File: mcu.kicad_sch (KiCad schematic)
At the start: 38 parts, among them SW1 SW_Push, SW2 SW_Push, SW3 SW_Push, SW4 SW_Push, U1 STM32H723VGTx, U13 BMI323, U14 AS5047P-ATST, U15 TCAN1044VDRQ1, X1 8MHz

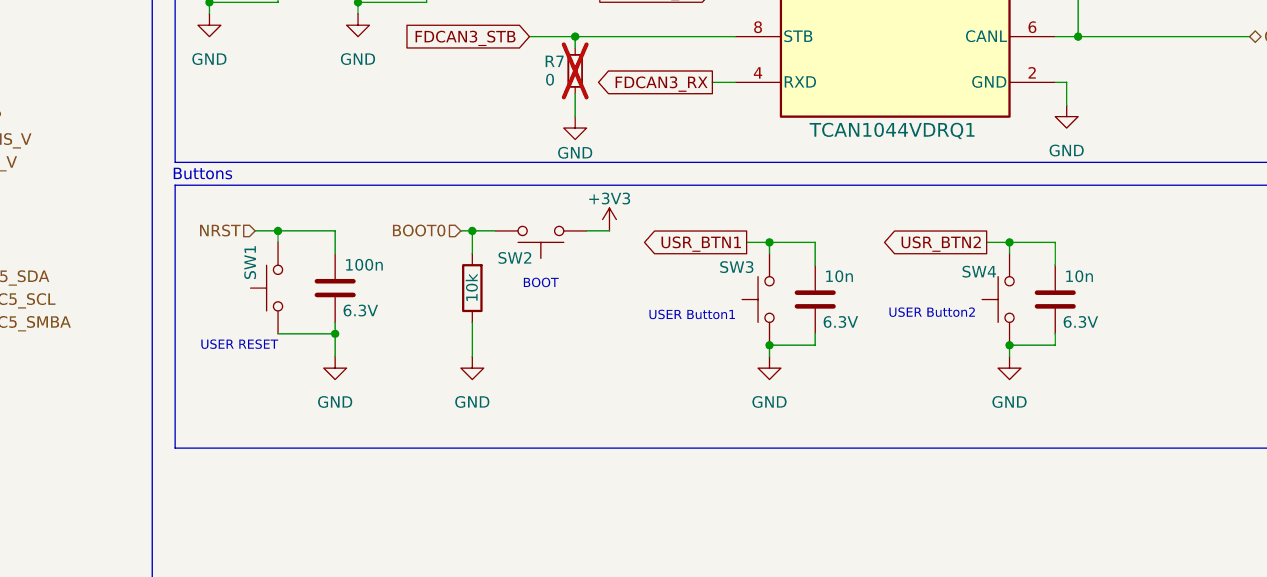
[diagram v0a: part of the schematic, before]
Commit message: Analog current filters were removed, some footprints were fixed and initial rough layout has been made.
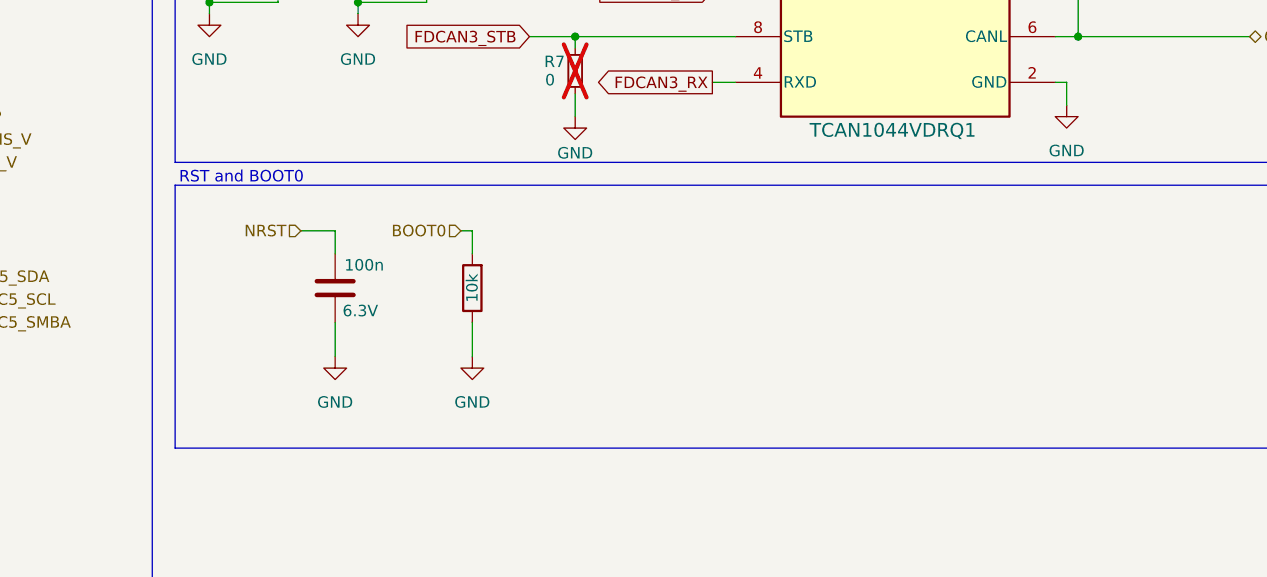
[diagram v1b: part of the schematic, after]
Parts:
- removed C81, C82: 10n, Capacitor_SMD:C_0201_0603Metric, symbol Device:C
- removed SW1, SW2, SW3, SW4: SW_Push, NanoGaN:SW_TS-1088_XNP, symbol Switch:SW_Push
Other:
- note added: "RST and BOOT0"
- note removed: "BOOT"
- note removed: "Buttons"
- note removed: "USER Button1"
- note removed: "USER Button2"
- note removed: "USER RESET"

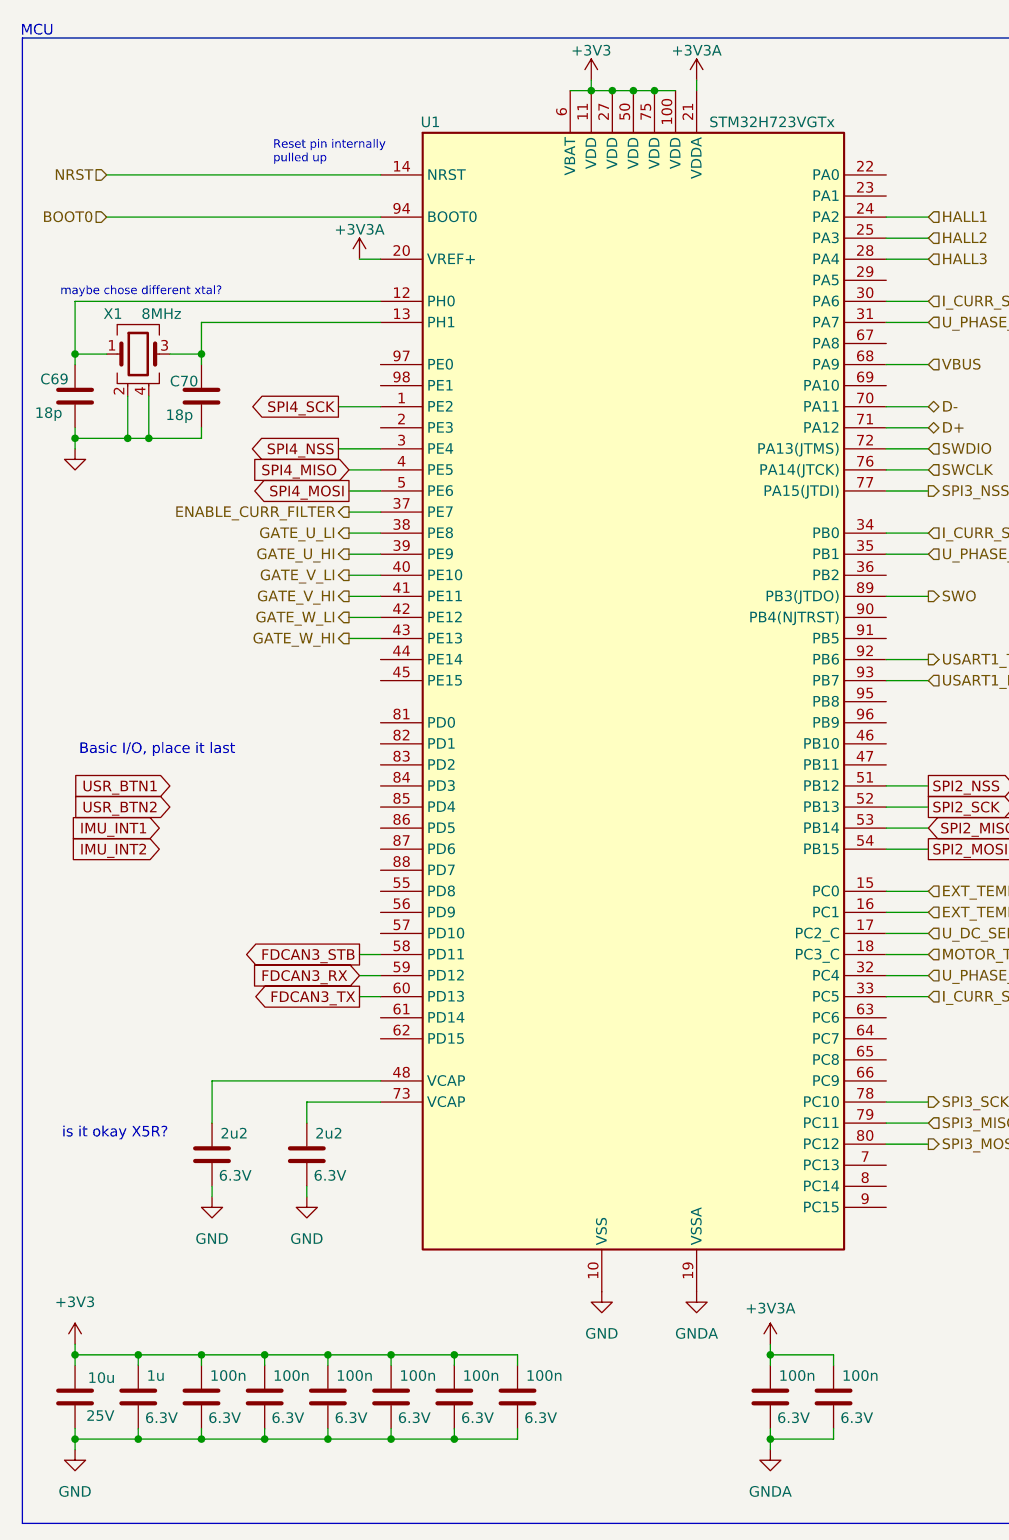
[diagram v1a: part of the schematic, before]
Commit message: pdf export and small fixes
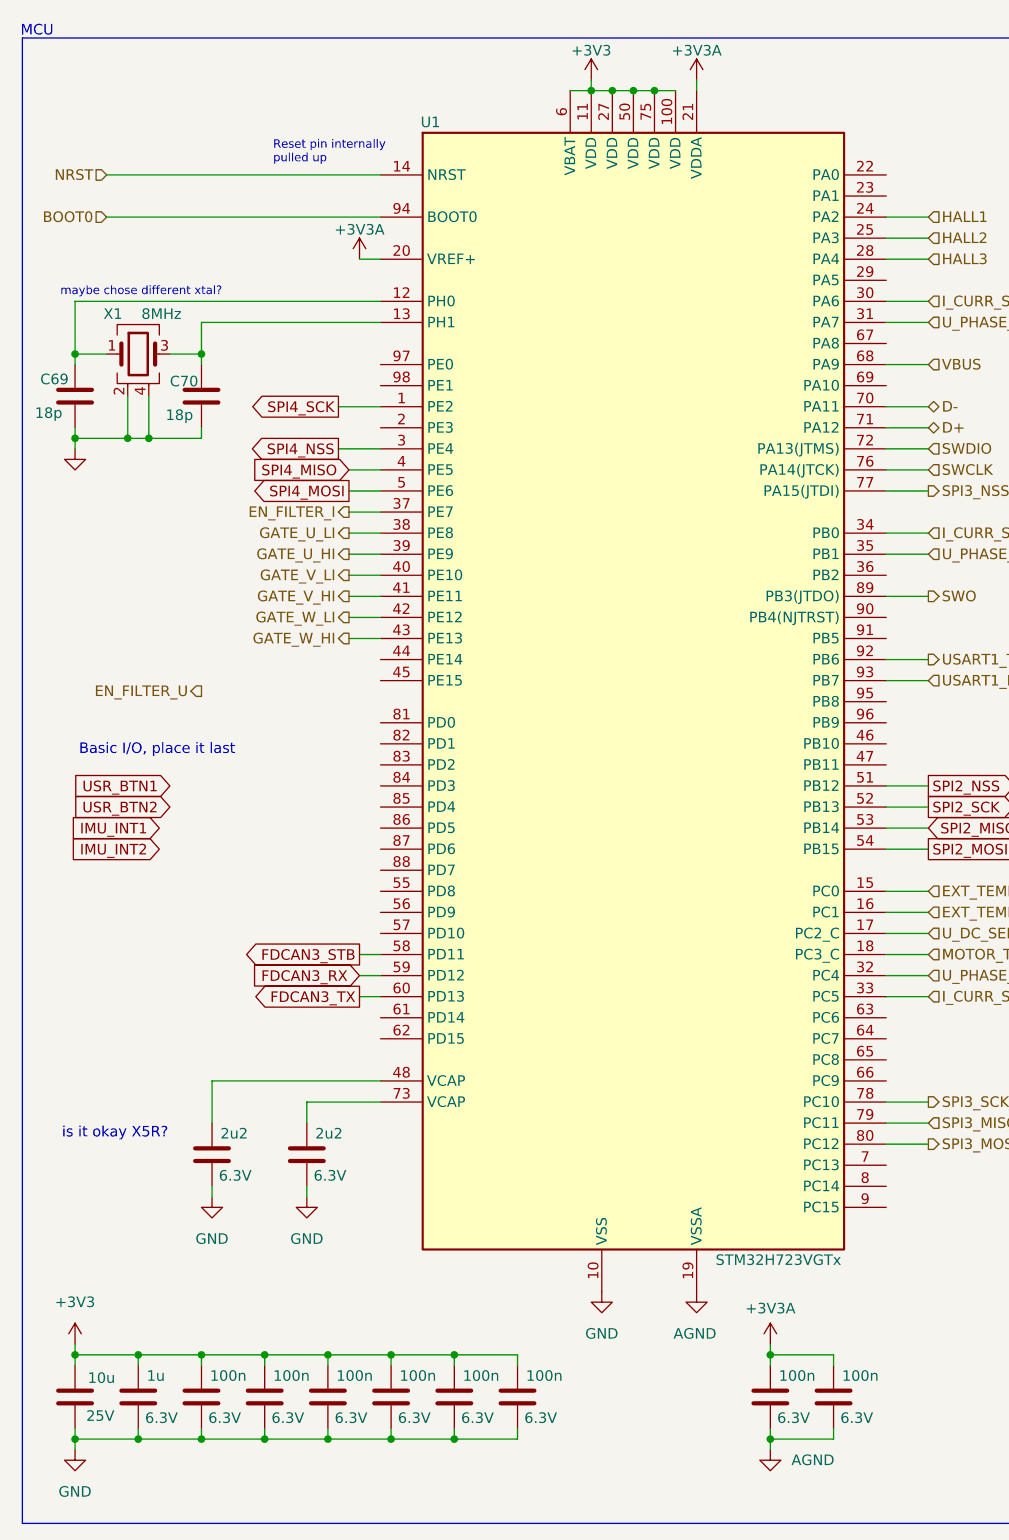
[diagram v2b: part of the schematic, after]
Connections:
- net ENABLE_CURR_FILTER renamed EN_FILTER_I
- net GNDA renamed AGND
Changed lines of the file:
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@@
 		)
 	)
+	(hierarchical_label "EN_FILTER_U"
+		(shape output)
+		(at 34.29 93.98 180)
+		(effects
+			(font
+				(size 1.27 1.27)
+			)
+			(justify right)
+		)
+	)
 	(hierarchical_label "SWCLK"
 		(shape input)
@@
 		)
 	)
-	(hierarchical_label "ENABLE_CURR_FILTER"
+	(hierarchical_label "EN_FILTER_I"
 		(shape output)
 		(at 52.07 72.39 180)
@@
 		(on_board yes)
 		(dnp no)
-		(fields_autoplaced yes)
 		(property "Reference" "#PWR04"
 			(at 93.98 172.72 0)
@@
 			)
 		)
-		(property "Value" "GNDA"
-			(at 93.98 171.45 0)
+		(property "Value" "AGND"
+			(at 91.186 171.45 0)
 			(effects
 				(font
 					(size 1.27 1.27)
 				)
+				(justify left)
 			)
 		)
@@
 			)
 		)
-		(property "Value" "GNDA"
-			(at 102.87 190.5 0)
+		(property "Value" "AGND"
+			(at 105.41 186.6899 0)
 			(effects
 				(font
 					(size 1.27 1.27)
 				)
+				(justify left)
 			)
 		)
@@
 		)
 		(property "Value" "STM32H723VGTx"
-			(at 95.504 25.4 0)
+			(at 96.266 162.56 0)
 			(effects
 				(font

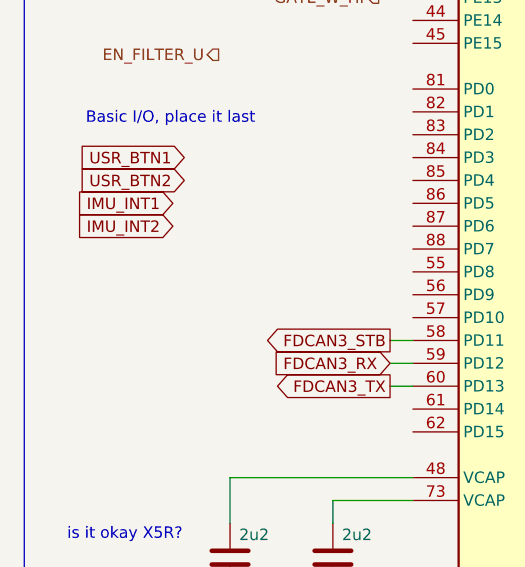
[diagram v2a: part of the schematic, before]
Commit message: Added PWM fan control
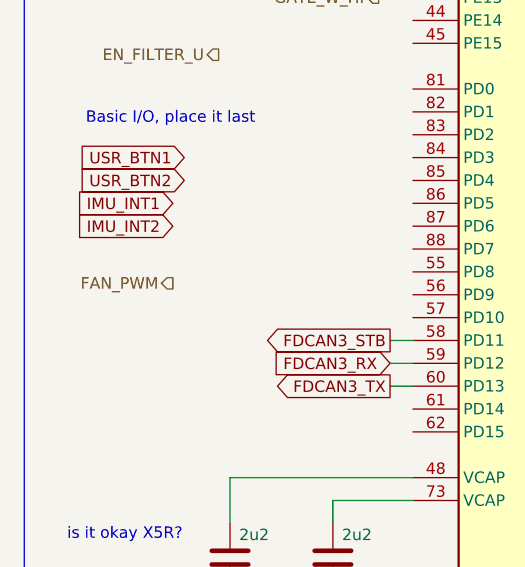
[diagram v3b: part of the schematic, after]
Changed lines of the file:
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@@
+		)
+	)
+	(hierarchical_label "FAN_PWM"
+		(shape output)
+		(at 29.21 119.38 180)
+		(effects
+			(font
+				(size 1.27 1.27)
+			)
+			(justify right)
 		)
 	)

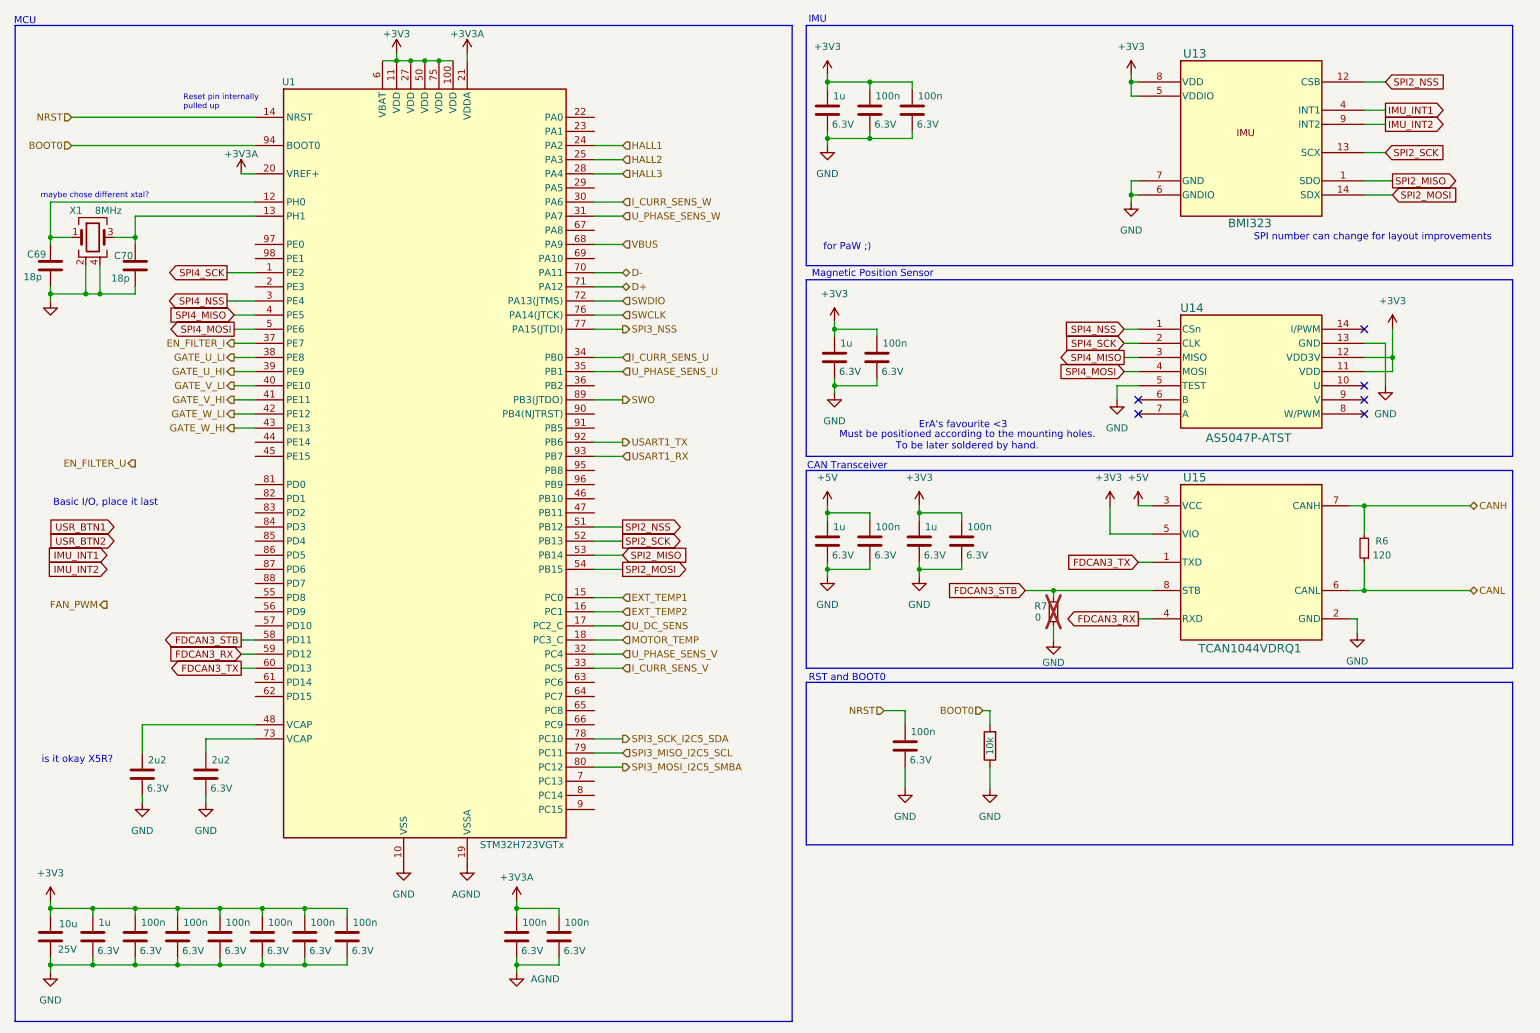
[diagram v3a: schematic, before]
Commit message: Differential pair naming added. Duplicate footprint problem fixed.
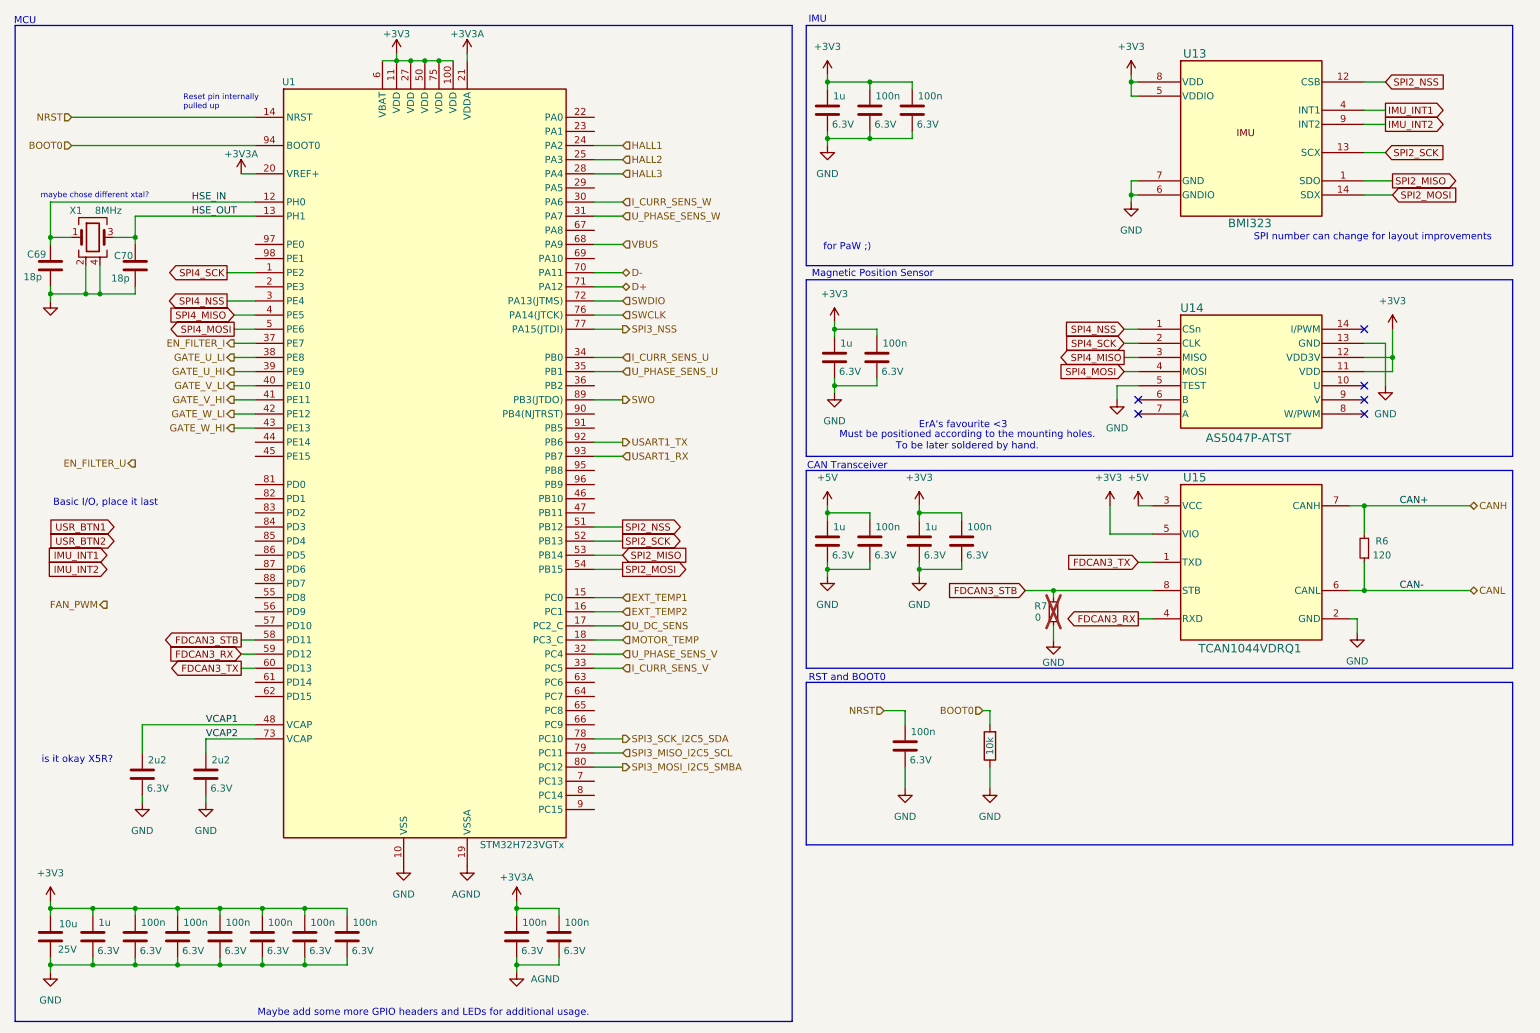
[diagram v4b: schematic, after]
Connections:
- net HSE_IN: now reaches C69.1, U1.12 (PH0), X1.1
- net VCAP1: now reaches C83.1, U1.48 (VCAP)
- net HSE_OUT: now reaches C70.1, U1.13 (PH1), X1.3
- net VCAP2: now reaches C84.1, U1.73 (VCAP)
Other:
- note added: "Maybe add some more GPIO headers and LEDs for additional usage."
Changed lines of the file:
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@@
+		)
+	)
+	(text "Maybe add some more GPIO headers and LEDs for additional usage."
+		(exclude_from_sim no)
+		(at 86.106 192.786 0)
+		(effects
+			(font
+				(size 1.27 1.27)
+			)
 		)
 	)
@@
 		)
 	)
+	(label "CAN-"
+		(at 261.62 116.84 0)
+		(effects
+			(font
+				(size 1.27 1.27)
+			)
+			(justify left bottom)
+		)
+	)
+	(label "VCAP2"
+		(at 46.99 143.51 0)
+		(effects
+			(font
+				(size 1.27 1.27)
+			)
+			(justify left bottom)
+		)
+	)
+	(label "VCAP1"
+		(at 46.99 140.97 0)
+		(effects
+			(font
+				(size 1.27 1.27)
+			)
+			(justify left bottom)
+		)
+	)
+	(label "HSE_OUT"
+		(at 44.45 49.53 0)
+		(effects
+			(font
+				(size 1.27 1.27)
+			)
+			(justify left bottom)
+		)
+	)
+	(label "HSE_IN"
+		(at 44.45 46.99 0)
+		(effects
+			(font
+				(size 1.27 1.27)
+			)
+			(justify left bottom)
+		)
+	)
+	(label "CAN+"
+		(at 261.62 101.6 0)
+		(effects
+			(font
+				(size 1.27 1.27)
+			)
+			(justify left bottom)
+		)
+	)
